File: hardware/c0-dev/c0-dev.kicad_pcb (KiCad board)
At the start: 2 copper layers, 316 parts, among them J1 RJHSE5385, J2 TAG_CONNECT, Q1 BSS138P, Q2 BSS138P, U1 LAN8720A, U10 ISO1540, U11 TMP117xxDRV, U12 AMS1117-3.3, U13 ADS1015IDGS, U14 ADS1015IDGS, U15 B0505S-1WR3, U16 ISO1540, U17 ADS1015IDGS, U18 ADS1015IDGS, U19 ADS1015IDGS, U2 TPS54360DDA, U20 ADS1015IDGS, U21 B0505S-1WR3, U22 ISO6741, U23 ISO6741, U24 ADS1220xPW, U25 ADS1220xPW, U26 B0505S-1WR3, U27 ISO1044BD, U28 TLP175A, U29 ISO1212, U3 TPS2378, U30 ISO1212, U31 ISO1212, U32 ISO1212, U4 TLP290, U5 B0505S-1WR3, U6 AMS1117-3.3, U7 W25Q128JVP, U8 RP2350A, U9 B0505S-1WR3, Y1 ABM8-272-T3 (12Mhz)

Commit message: i2c address check
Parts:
- added C116: 10uF, Capacitor_SMD:C_0805_2012Metric, F.Cu at (180.1, 61.6)
- added C117: 0.1uF, Capacitor_SMD:C_0402_1005Metric, F.Cu at (183.7, 61.1)
- added C118: 10uF, Capacitor_SMD:C_0805_2012Metric, F.Cu at (180.1, 64.6)
- added C119: 0.1uF, Capacitor_SMD:C_0402_1005Metric, F.Cu at (183.7, 63.1)
- added C120: 10uF, Capacitor_SMD:C_0805_2012Metric, F.Cu at (180.1, 67.7)
- added C121: 0.1uF, Capacitor_SMD:C_0402_1005Metric, F.Cu at (183.7, 65.1)
- added C122: 1uF, Capacitor_SMD:C_0603_1608Metric, F.Cu at (200.2, 89.1)
- added C123: 2.2uF, Capacitor_SMD:C_0603_1608Metric, F.Cu at (200.2, 91.6)
- added C124: 10uF, Capacitor_SMD:C_1206_3216Metric, F.Cu at (201.0, 94.6)
- added C125: 1uF, Capacitor_SMD:C_0603_1608Metric, F.Cu at (179.5, 81.9)
- added C126: 2.2uF, Capacitor_SMD:C_0603_1608Metric, F.Cu at (179.5, 84.4)
- added C127: 10uF, Capacitor_SMD:C_1206_3216Metric, F.Cu at (180.3, 87.4)
- added C128: 1uF, Capacitor_SMD:C_0603_1608Metric, F.Cu at (218.8, 71.9)
- added C129: 2.2uF, Capacitor_SMD:C_0603_1608Metric, F.Cu at (218.8, 74.4)
- added C130: 10uF, Capacitor_SMD:C_1206_3216Metric, F.Cu at (219.7, 77.4)
- added C131: 1uF, Capacitor_SMD:C_0603_1608Metric, F.Cu at (179.5, 99.1)
- added C132: 2.2uF, Capacitor_SMD:C_0603_1608Metric, F.Cu at (179.5, 101.6)
- added C133: 10uF, Capacitor_SMD:C_1206_3216Metric, F.Cu at (180.3, 104.5)
- added C134: 1uF, Capacitor_SMD:C_0603_1608Metric, F.Cu at (200.2, 71.9)
- added C135: 2.2uF, Capacitor_SMD:C_0603_1608Metric, F.Cu at (200.2, 74.4)
- added C136: 10uF, Capacitor_SMD:C_1206_3216Metric, F.Cu at (201.0, 77.4)
- added C137: 1uF, Capacitor_SMD:C_0603_1608Metric, F.Cu at (200.2, 54.7)
- added C138: 2.2uF, Capacitor_SMD:C_0603_1608Metric, F.Cu at (200.2, 57.3)
- added C139: 10uF, Capacitor_SMD:C_1206_3216Metric, F.Cu at (201.0, 60.2)
- added C140: 1uF, Capacitor_SMD:C_0603_1608Metric, F.Cu at (218.8, 89.1)
- added C141: 2.2uF, Capacitor_SMD:C_0603_1608Metric, F.Cu at (218.8, 91.6)
- added C142: 10uF, Capacitor_SMD:C_1206_3216Metric, F.Cu at (219.7, 94.6)
- added C143: 1uF, Capacitor_SMD:C_0603_1608Metric, F.Cu at (218.8, 54.7)
- added C144: 2.2uF, Capacitor_SMD:C_0603_1608Metric, F.Cu at (218.8, 57.3)
- added C145: 10uF, Capacitor_SMD:C_1206_3216Metric, F.Cu at (219.7, 60.2)
- added D36: SS14, Diode_SMD:D_SMA, F.Cu at (170.6, 69.0)
- added D37: SS14, Diode_SMD:D_SMA, F.Cu at (194.2, 90.1)
- added D38: PTVS30VP1UP, Diode_SMD:D_SOD-128, F.Cu at (193.8, 94.4)
- added D39: SS14, Diode_SMD:D_SMA, F.Cu at (173.5, 82.9)
- added D40: PTVS30VP1UP, Diode_SMD:D_SOD-128, F.Cu at (173.1, 87.2)
- added D41: SS14, Diode_SMD:D_SMA, F.Cu at (212.8, 73.0)
- added D42: PTVS30VP1UP, Diode_SMD:D_SOD-128, F.Cu at (212.5, 77.3)
- added D43: SS14, Diode_SMD:D_SMA, F.Cu at (173.5, 100.1)
- added D44: PTVS30VP1UP, Diode_SMD:D_SOD-128, F.Cu at (173.1, 104.4)
- added D45: SS14, Diode_SMD:D_SMA, F.Cu at (194.2, 73.0)
- added D46: PTVS30VP1UP, Diode_SMD:D_SOD-128, F.Cu at (193.8, 77.3)
- added D47: SS14, Diode_SMD:D_SMA, F.Cu at (194.2, 55.8)
- added D48: PTVS30VP1UP, Diode_SMD:D_SOD-128, F.Cu at (193.8, 60.1)
- added D49: SS14, Diode_SMD:D_SMA, F.Cu at (212.8, 90.1)
- added D50: PTVS30VP1UP, Diode_SMD:D_SOD-128, F.Cu at (212.5, 94.4)
- added D51: SS14, Diode_SMD:D_SMA, F.Cu at (212.8, 55.8)
- added D52: PTVS30VP1UP, Diode_SMD:D_SOD-128, F.Cu at (212.5, 60.1)
- added FB8: 600Ω@100MHz, Inductor_SMD:L_0603_1608Metric, F.Cu at (179.9, 70.4)
- added R103: 2k, Resistor_SMD:R_1206_3216Metric, F.Cu at (170.0, 116.1)
- added R109: 560, Resistor_SMD:R_0402_1005Metric, F.Cu at (174.3, 117.4)
- added R113: 2k, Resistor_SMD:R_1206_3216Metric, F.Cu at (170.0, 119.4)
- added R113: 1k, Resistor_SMD:R_0402_1005Metric, F.Cu at (176.4, 61.1)
- added R114: 1k, Resistor_SMD:R_0402_1005Metric, F.Cu at (176.4, 63.1)
- added R115: 1k, Resistor_SMD:R_0402_1005Metric, F.Cu at (176.4, 65.1)
- added R116: 1k, Resistor_SMD:R_0402_1005Metric, F.Cu at (176.4, 67.1)
- added R117: 1k, Resistor_SMD:R_0402_1005Metric, F.Cu at (176.4, 69.1)
- added R118: 1k, Resistor_SMD:R_0402_1005Metric, F.Cu at (176.4, 71.1)
- added R119: 10k, Resistor_SMD:R_0402_1005Metric, F.Cu at (188.6, 82.3)
- added R120: 715k, Resistor_SMD:R_0402_1005Metric, F.Cu at (188.6, 84.3)
- added R121: 20k, Resistor_SMD:R_0402_1005Metric, F.Cu at (188.6, 86.3)
- added R122: 30.1k, Resistor_SMD:R_0402_1005Metric, F.Cu at (188.6, 88.2)
- added R123: 0, Resistor_SMD:R_0402_1005Metric, F.Cu at (188.6, 90.2)
- added R124: 10k, Resistor_SMD:R_0402_1005Metric, F.Cu at (188.6, 92.2)
- added R125: 12k, Resistor_SMD:R_0402_1005Metric, F.Cu at (188.6, 94.2)
- added R126: 62k, Resistor_SMD:R_0402_1005Metric, F.Cu at (168.0, 75.1)
- added R127: 715k, Resistor_SMD:R_0402_1005Metric, F.Cu at (168.0, 77.1)
- added R128: 20k, Resistor_SMD:R_0402_1005Metric, F.Cu at (168.0, 79.0)
- added R129: 30.1k, Resistor_SMD:R_0402_1005Metric, F.Cu at (168.0, 81.0)
- added R13: 2M, Resistor_SMD:R_1206_3216Metric, F.Cu at (170.0, 132.9)
- added R130: 0, Resistor_SMD:R_0402_1005Metric, F.Cu at (168.0, 83.0)
- added R131: 10k, Resistor_SMD:R_0402_1005Metric, F.Cu at (168.0, 85.0)
- added R132: 12k, Resistor_SMD:R_0402_1005Metric, F.Cu at (168.0, 87.0)
- added R133: 62k, Resistor_SMD:R_0402_1005Metric, F.Cu at (207.3, 65.1)
- added R134: 715k, Resistor_SMD:R_0402_1005Metric, F.Cu at (207.3, 67.1)
- added R135: 20k, Resistor_SMD:R_0402_1005Metric, F.Cu at (207.3, 69.1)
- added R136: 30.1k, Resistor_SMD:R_0402_1005Metric, F.Cu at (207.3, 71.1)
- added R137: 0, Resistor_SMD:R_0402_1005Metric, F.Cu at (207.3, 73.0)
- added R138: 10k, Resistor_SMD:R_0402_1005Metric, F.Cu at (207.3, 75.0)
- added R139: 12k, Resistor_SMD:R_0402_1005Metric, F.Cu at (207.3, 77.0)
- added R140: 62k, Resistor_SMD:R_0402_1005Metric, F.Cu at (168.0, 92.3)
- added R141: 715k, Resistor_SMD:R_0402_1005Metric, F.Cu at (168.0, 94.2)
- added R142: 20k, Resistor_SMD:R_0402_1005Metric, F.Cu at (168.0, 96.2)
- added R143: 30.1k, Resistor_SMD:R_0402_1005Metric, F.Cu at (168.0, 98.2)
- added R144: 0, Resistor_SMD:R_0402_1005Metric, F.Cu at (168.0, 100.2)
- added R145: 10k, Resistor_SMD:R_0402_1005Metric, F.Cu at (168.0, 102.2)
- added R146: 12k, Resistor_SMD:R_0402_1005Metric, F.Cu at (168.0, 104.2)
- added R147: 62k, Resistor_SMD:R_0402_1005Metric, F.Cu at (188.6, 65.1)
- added R148: 715k, Resistor_SMD:R_0402_1005Metric, F.Cu at (188.6, 67.1)
- added R149: 20k, Resistor_SMD:R_0402_1005Metric, F.Cu at (188.6, 69.1)
- added R150: 30.1k, Resistor_SMD:R_0402_1005Metric, F.Cu at (188.6, 71.1)
- added R151: 0, Resistor_SMD:R_0402_1005Metric, F.Cu at (188.6, 73.0)
- added R152: 10k, Resistor_SMD:R_0402_1005Metric, F.Cu at (188.6, 75.0)
- added R153: 12k, Resistor_SMD:R_0402_1005Metric, F.Cu at (188.6, 77.0)
- added R154: 62k, Resistor_SMD:R_0402_1005Metric, F.Cu at (188.6, 47.9)
- added R155: 715k, Resistor_SMD:R_0402_1005Metric, F.Cu at (188.6, 49.9)
- added R156: 20k, Resistor_SMD:R_0402_1005Metric, F.Cu at (188.6, 51.9)
- added R157: 30.1k, Resistor_SMD:R_0402_1005Metric, F.Cu at (188.6, 53.9)
- added R158: 0, Resistor_SMD:R_0402_1005Metric, F.Cu at (188.6, 55.9)
- added R159: 10k, Resistor_SMD:R_0402_1005Metric, F.Cu at (188.6, 57.8)
- added R160: 12k, Resistor_SMD:R_0402_1005Metric, F.Cu at (188.6, 59.8)
- added R161: 62k, Resistor_SMD:R_0402_1005Metric, F.Cu at (207.3, 82.3)
- added R162: 715k, Resistor_SMD:R_0402_1005Metric, F.Cu at (207.3, 84.3)
- added R163: 20k, Resistor_SMD:R_0402_1005Metric, F.Cu at (207.3, 86.3)
- added R164: 30.1k, Resistor_SMD:R_0402_1005Metric, F.Cu at (207.3, 88.2)
- added R165: 0, Resistor_SMD:R_0402_1005Metric, F.Cu at (207.3, 90.2)
- added R166: 10k, Resistor_SMD:R_0402_1005Metric, F.Cu at (207.3, 92.2)
- added R167: 12k, Resistor_SMD:R_0402_1005Metric, F.Cu at (207.3, 94.2)
- added R168: 62k, Resistor_SMD:R_0402_1005Metric, F.Cu at (207.3, 47.9)
- added R169: 715k, Resistor_SMD:R_0402_1005Metric, F.Cu at (207.3, 49.9)
- added R170: 20k, Resistor_SMD:R_0402_1005Metric, F.Cu at (207.3, 51.9)
- added R171: 30.1k, Resistor_SMD:R_0402_1005Metric, F.Cu at (207.3, 53.9)
- added R172: 0, Resistor_SMD:R_0402_1005Metric, F.Cu at (207.3, 55.9)
- added R173: 10k, Resistor_SMD:R_0402_1005Metric, F.Cu at (207.3, 57.8)
- added R174: 12k, Resistor_SMD:R_0402_1005Metric, F.Cu at (207.3, 59.8)
- added R175: 62k, Resistor_SMD:R_0402_1005Metric, F.Cu at (184.4, 131.3)
- added R41: 1k, Resistor_SMD:R_0402_1005Metric, F.Cu at (178.0, 127.3)
- added R49: 2k, Resistor_SMD:R_1206_3216Metric, F.Cu at (179.3, 124.7)
- added R67: 1.6k, Resistor_SMD:R_0402_1005Metric, F.Cu at (173.1, 127.3)
- added R71: 160, Resistor_SMD:R_0805_2012Metric, F.Cu at (169.4, 127.8)
- added R72: 0, Resistor_SMD:R_1206_3216Metric, F.Cu at (170.0, 124.7)
- added R78: 1k, Resistor_SMD:R_0402_1005Metric, F.Cu at (184.8, 115.4)
- added R82: 2k, Resistor_SMD:R_1206_3216Metric, F.Cu at (180.5, 116.1)
- added R86: 1M, Resistor_SMD:R_0402_1005Metric, F.Cu at (184.8, 117.4)
- added R88: 2k, Resistor_SMD:R_1206_3216Metric, F.Cu at (180.5, 119.4)
- added R91: 1k, Resistor_SMD:R_0402_1005Metric, F.Cu at (178.0, 134.3)
- added R92: 120R, Resistor_SMD:R_0805_2012Metric, F.Cu at (178.7, 131.8)
- added R99: 560, Resistor_SMD:R_0402_1005Metric, F.Cu at (174.3, 115.4)
- added U33: B0505S-1WR3, Converter_DCDC:Converter_DCDC_Murata_MEE1SxxxxSC_THT, F.Cu at (168.6, 49.9)
- added U34: ISO1540, Package_SO:SOIC-8_3.9x4.9mm_P1.27mm, F.Cu at (170.7, 63.5)
- added U35: TCA9555PWR, Package_SO:TSSOP-24_4.4x7.8mm_P0.65mm, F.Cu at (179.1, 51.6)
- added U36: TPS26600PWP, Package_SO:HTSSOP-16-1EP_4.4x5mm_P0.65mm_EP3.4x5mm_Mask2.66x2.46mm_ThermalVias, F.Cu at (194.9, 84.6)
- added U37: TPS26600PWP, Package_SO:HTSSOP-16-1EP_4.4x5mm_P0.65mm_EP3.4x5mm_Mask2.66x2.46mm_ThermalVias, F.Cu at (174.2, 77.4)
- added U38: TPS26600PWP, Package_SO:HTSSOP-16-1EP_4.4x5mm_P0.65mm_EP3.4x5mm_Mask2.66x2.46mm_ThermalVias, F.Cu at (213.5, 67.4)
- added U39: TPS26600PWP, Package_SO:HTSSOP-16-1EP_4.4x5mm_P0.65mm_EP3.4x5mm_Mask2.66x2.46mm_ThermalVias, F.Cu at (174.2, 94.6)
- added U40: TPS26600PWP, Package_SO:HTSSOP-16-1EP_4.4x5mm_P0.65mm_EP3.4x5mm_Mask2.66x2.46mm_ThermalVias, F.Cu at (194.9, 67.4)
- added U41: TPS26600PWP, Package_SO:HTSSOP-16-1EP_4.4x5mm_P0.65mm_EP3.4x5mm_Mask2.66x2.46mm_ThermalVias, F.Cu at (194.9, 50.2)
- added U42: TPS26600PWP, Package_SO:HTSSOP-16-1EP_4.4x5mm_P0.65mm_EP3.4x5mm_Mask2.66x2.46mm_ThermalVias, F.Cu at (213.5, 84.6)
- added U43: TPS26600PWP, Package_SO:HTSSOP-16-1EP_4.4x5mm_P0.65mm_EP3.4x5mm_Mask2.66x2.46mm_ThermalVias, F.Cu at (213.5, 50.2)
- R105, R95: value 560 -> 1k
- R17: value 33R -> 75R
- R19: value 68.1k -> 33R
- R20: value 25k -> 68.1k
- R21: value 63.4R -> 25k
- R22: value 6.34k -> 63.4R
- R23: value 60.4k -> 6.34k
- R24: value 11.5k -> 60.4k
- R25: value 1k -> 11.5k
- R26: value 10k -> 1k
- R27, R74: value 1k -> 10k
- R28: value 33 -> 1k
- R29: value 1k -> 33
- R30: value DNP -> 1k
- R31: value 0 -> DNP
- R32: value 27 -> 0
- R33, R36: value 1k -> 27
- R35: value 27 -> 1k
- R57: value 1k -> 1M
- R63: value 1.6k -> 1k
- R90, R93: value 1k -> 0
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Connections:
- R100 pad 1: /Digital Input/IN1 -> /Digital Input/IN0
- R100 pad 2: Net-(U29-SENSE2) -> Net-(U29-SENSE1)
- R101 pad 1: /Digital Input/IN2 -> /Digital Input/IN1
- R101 pad 2: Net-(U30-SENSE1) -> Net-(U29-SENSE2)
- R102 pad 1: /Digital Input/IN3 -> /Digital Input/IN2
- R102 pad 2: Net-(U30-SENSE2) -> Net-(U30-SENSE1)
- R104 pad 2: Net-(U32-EN) -> Net-(U31-EN)
- R105 pad 1: Net-(U31-IN1) -> /Digital Input/+3.3V_ISO
- R105 pad 2: Net-(U31-SENSE1) -> Net-(U32-EN)
- R106 pad 1: Net-(U31-IN2) -> Net-(U31-IN1)
- R106 pad 2: Net-(U31-SENSE2) -> Net-(U31-SENSE1)
- R107 pad 1: Net-(U32-IN1) -> Net-(U31-IN2)
- R107 pad 2: Net-(U32-SENSE1) -> Net-(U31-SENSE2)
- R108 pad 1: Net-(U32-IN2) -> Net-(U32-IN1)
- R108 pad 2: Net-(U32-SENSE2) -> Net-(U32-SENSE1)
- R110 pad 1: /Digital Input/IN5 -> /Digital Input/IN4
- R110 pad 2: Net-(U31-SENSE2) -> Net-(U31-SENSE1)
- R111 pad 1: /Digital Input/IN6 -> /Digital Input/IN5
- R111 pad 2: Net-(U32-SENSE1) -> Net-(U31-SENSE2)
- R112 pad 1: /Digital Input/IN7 -> /Digital Input/IN6
- R112 pad 2: Net-(U32-SENSE2) -> Net-(U32-SENSE1)
- R14 pad 1: Net-(C9-Pad2) -> Net-(C8-Pad2)
- R15 pad 1: Net-(C10-Pad2) -> Net-(C9-Pad2)
- R16 pad 1: Net-(C11-Pad2) -> Net-(C10-Pad2)
- R17 pad 1: /Ethernet/LED1 -> Net-(C11-Pad2)
- R17 pad 2: Net-(J1-Pad11) -> Earth
- R18 pad 1: /Ethernet/LED2 -> /Ethernet/LED1
- R18 pad 2: Net-(J1-Pad9) -> Net-(J1-Pad11)
- R19 pad 1: Net-(U2-RT/CLK) -> /Ethernet/LED2
- R19 pad 2: GND_ISO -> Net-(J1-Pad9)
- R20 pad 1: Net-(U3-DEN) -> Net-(U2-RT/CLK)
- R20 pad 2: +POE -> GND_ISO
- R21 pad 1: -POE -> Net-(U3-DEN)
- R21 pad 2: Net-(U3-CLS) -> +POE
- R22 pad 1: Net-(U2-COMP) -> -POE
- R22 pad 2: Net-(C19-Pad1) -> Net-(U3-CLS)
- R23 pad 1: +5V_ISO -> Net-(U2-COMP)
- R23 pad 2: Net-(R23-Pad2) -> Net-(C19-Pad1)
- R24 pad 1: Net-(R23-Pad2) -> +5V_ISO
- R24 pad 2: GND_ISO -> Net-(R24-Pad2)
- R25 pad 1: GND_ISO -> Net-(R24-Pad2)
- R25 pad 2: Net-(U3-APD) -> GND_ISO
- R26 pad 1: +POE -> GND_ISO
- R26 pad 2: Net-(R26-Pad2) -> Net-(U3-APD)
- R27 pad 1: +3.3V -> +POE
- R27 pad 2: /Power/T2P -> Net-(R27-Pad2)
- R28 pad 2: /MCU/VREG_AVDD -> /Power/T2P
- R29 pad 1: Net-(R29-Pad1) -> +3.3V
- R29 pad 2: /MCU/~{QSPI_SS} -> /MCU/VREG_AVDD
- R30 pad 1: +3.3V -> Net-(R30-Pad1)
- R30 pad 2: Net-(U7-~{CS}) -> /MCU/~{QSPI_SS}
- R31 pad 1: Net-(U7-~{CS}) -> +3.3V
- R31 pad 2: /MCU/~{QSPI_SS} -> Net-(U7-~{CS})
- R32 pad 1: /MCU/USB_D+ -> Net-(U7-~{CS})
- R32 pad 2: Net-(U8-USB_DP) -> /MCU/~{QSPI_SS}
- R33 pad 1: Net-(C39-Pad2) -> /MCU/USB_D+
- R33 pad 2: Net-(U8-XOUT) -> Net-(U8-USB_DP)
- R34 pad 1: /MCU/~{RST} -> Net-(C39-Pad2)
- R34 pad 2: +3.3V -> Net-(U8-XOUT)
- R35 pad 1: /MCU/USB_D- -> /MCU/~{RST}
- R35 pad 2: Net-(U8-USB_DM) -> +3.3V
- R36 pad 1: /frontend_temp/SCL -> /MCU/USB_D-
- R36 pad 2: Net-(U11-ADD0) -> Net-(U8-USB_DM)
- R37 pad 2: /frontend_temp/+3.3V -> Net-(U11-ADD0)
- R38 pad 1: /frontend_temp/SDA -> /frontend_temp/SCL
- R39 pad 1: /frontend_temp/GND -> /frontend_temp/SDA
- R39 pad 2: Net-(U13-ADDR) -> /frontend_temp/+3.3V
- R40 pad 1: /frontend_temp/+3.3V -> /frontend_temp/GND
- R40 pad 2: Net-(U14-ADDR) -> Net-(U13-ADDR)
- R42 pad 1: /frontend_temp/TC0+ -> /frontend_temp/TC0-
- R42 pad 2: Net-(D6A-K3A4) -> Net-(D6B-K1A2)
- R43 pad 1: /frontend_temp/TC1- -> /frontend_temp/TC0+
- R43 pad 2: Net-(D7B-K1A2) -> Net-(D6A-K3A4)
- R44 pad 1: /frontend_temp/TC1+ -> /frontend_temp/TC1-
- R44 pad 2: Net-(D7A-K3A4) -> Net-(D7B-K1A2)
- R45 pad 1: /frontend_temp/TC2- -> /frontend_temp/TC1+
- R45 pad 2: Net-(D8B-K1A2) -> Net-(D7A-K3A4)
- R46 pad 1: /frontend_temp/TC2+ -> /frontend_temp/TC2-
- R46 pad 2: Net-(D8A-K3A4) -> Net-(D8B-K1A2)
- R47 pad 1: /frontend_temp/TC3- -> /frontend_temp/TC2+
- R47 pad 2: Net-(D9B-K1A2) -> Net-(D8A-K3A4)
- R48 pad 1: /frontend_temp/TC3+ -> /frontend_temp/TC3-
- R48 pad 2: Net-(D9A-K3A4) -> Net-(D9B-K1A2)
- R50 pad 1: /frontend_temp/GND -> /frontend_temp/TC0-
- R50 pad 2: /frontend_temp/TC0+ -> /frontend_temp/+3.3V
- R51 pad 1: /frontend_temp/TC1- -> /frontend_temp/GND
- R51 pad 2: /frontend_temp/+3.3V -> /frontend_temp/TC0+
- R52 pad 1: /frontend_temp/GND -> /frontend_temp/TC1-
- R52 pad 2: /frontend_temp/TC1+ -> /frontend_temp/+3.3V
- R53 pad 1: /frontend_temp/TC2- -> /frontend_temp/GND
- R53 pad 2: /frontend_temp/+3.3V -> /frontend_temp/TC1+
- R54 pad 1: /frontend_temp/GND -> /frontend_temp/TC2-
- R54 pad 2: /frontend_temp/TC2+ -> /frontend_temp/+3.3V
- R55 pad 1: /frontend_temp/TC3- -> /frontend_temp/GND
- R55 pad 2: /frontend_temp/+3.3V -> /frontend_temp/TC2+
- R56 pad 1: /frontend_temp/GND -> /frontend_temp/TC3-
- R56 pad 2: /frontend_temp/TC3+ -> /frontend_temp/+3.3V
- R57 pad 1: /frontend_420/SCL -> /frontend_temp/GND
- R57 pad 2: /frontend_420/+5V -> /frontend_temp/TC3+
- R58 pad 1: /frontend_420/SDA -> /frontend_420/SCL
- R59 pad 1: /frontend_420/GND -> /frontend_420/SDA
- R59 pad 2: Net-(U17-ADDR) -> /frontend_420/+5V
- R60 pad 1: /frontend_420/+5V -> /frontend_420/GND
- R60 pad 2: Net-(U18-ADDR) -> Net-(U17-ADDR)
- R61 pad 1: /frontend_420/SCL -> /frontend_420/+5V
- R61 pad 2: Net-(U19-ADDR) -> Net-(U18-ADDR)
- R62 pad 1: /frontend_420/SDA -> /frontend_420/SCL
- R62 pad 2: Net-(U20-ADDR) -> Net-(U19-ADDR)
- R63 pad 1: Net-(U17-AIN0) -> /frontend_420/SDA
- R63 pad 2: Net-(D19A-K3A4) -> Net-(U20-ADDR)
- R64 pad 1: Net-(U18-AIN0) -> Net-(U17-AIN0)
- R64 pad 2: Net-(D20A-K3A4) -> Net-(D19A-K3A4)
- R65 pad 1: Net-(U19-AIN0) -> Net-(U18-AIN0)
- R65 pad 2: Net-(D21A-K3A4) -> Net-(D20A-K3A4)
- R66 pad 1: Net-(U20-AIN0) -> Net-(U19-AIN0)
- R66 pad 2: Net-(D22A-K3A4) -> Net-(D21A-K3A4)
- R68 pad 1: Net-(D20A-K3A4) -> Net-(D19A-K3A4)
- R69 pad 1: Net-(D21A-K3A4) -> Net-(D20A-K3A4)
- R70 pad 1: Net-(D22A-K3A4) -> Net-(D21A-K3A4)
- R73 pad 2: /frontend_bridge/~{CS1_ISO} -> /frontend_bridge/~{CS0_ISO}
- R74 pad 1: Net-(U22-EN2) -> GND_ISO
- R74 pad 2: /frontend_bridge/+5V -> /frontend_bridge/~{CS1_ISO}
- R75 pad 1: Net-(U23-EN2) -> Net-(U22-EN2)
- R76 pad 1: /frontend_bridge/GND -> Net-(U23-EN2)
- R76 pad 2: Net-(U24-CLK) -> /frontend_bridge/+5V
- R77 pad 2: Net-(U25-CLK) -> Net-(U24-CLK)
- R79 pad 1: /frontend_bridge/B0- -> /frontend_bridge/B0+
- R79 pad 2: /frontend_bridge/AIN20 -> /frontend_bridge/AIN10
- R80 pad 1: /frontend_bridge/B1+ -> /frontend_bridge/B0-
- R80 pad 2: /frontend_bridge/AIN11 -> /frontend_bridge/AIN20
- R81 pad 1: /frontend_bridge/B1- -> /frontend_bridge/B1+
- R81 pad 2: /frontend_bridge/AIN21 -> /frontend_bridge/AIN11
- R83 pad 1: /frontend_bridge/GND -> /frontend_bridge/B0+
- R83 pad 2: /frontend_bridge/B0- -> /frontend_bridge/+5V
- R84 pad 1: /frontend_bridge/B1+ -> /frontend_bridge/GND
- R84 pad 2: /frontend_bridge/+5V -> /frontend_bridge/B0-
- R85 pad 1: /frontend_bridge/GND -> /frontend_bridge/B1+
- R85 pad 2: /frontend_bridge/B1- -> /frontend_bridge/+5V
- R87 pad 1: /frontend_bridge/B1_5V+ -> /frontend_bridge/B0_5V+
- R87 pad 2: /frontend_bridge/+5V_SENSE1 -> /frontend_bridge/+5V_SENSE0
- R89 pad 1: /frontend_bridge/B1_GND -> /frontend_bridge/B0_GND
- R90 pad 1: Net-(R90-Pad1) -> /frontend_bridge/B1_GND
- R90 pad 2: /CAN/TERM_EN -> /frontend_bridge/GND
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
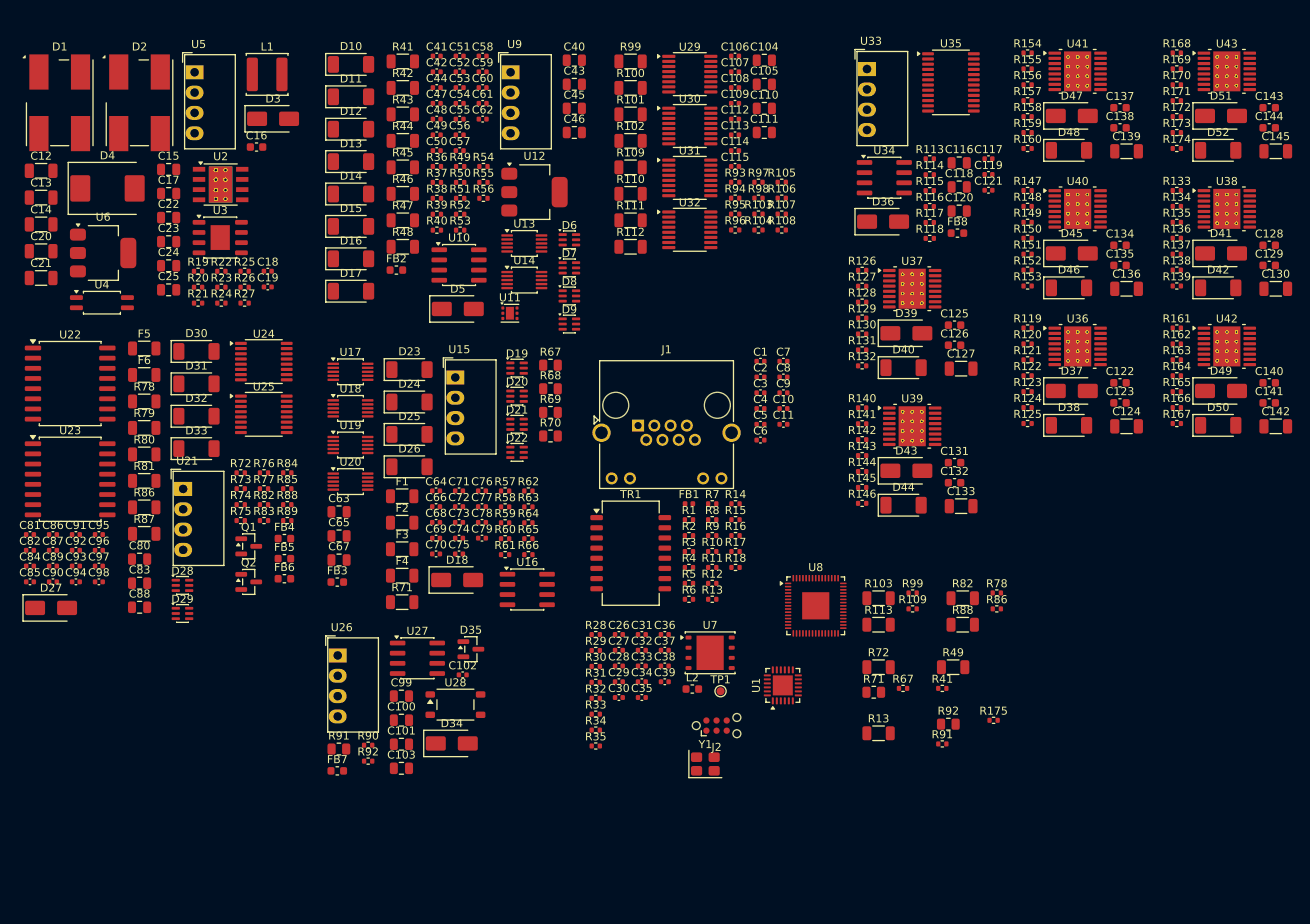
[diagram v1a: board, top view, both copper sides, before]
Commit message: added connectors
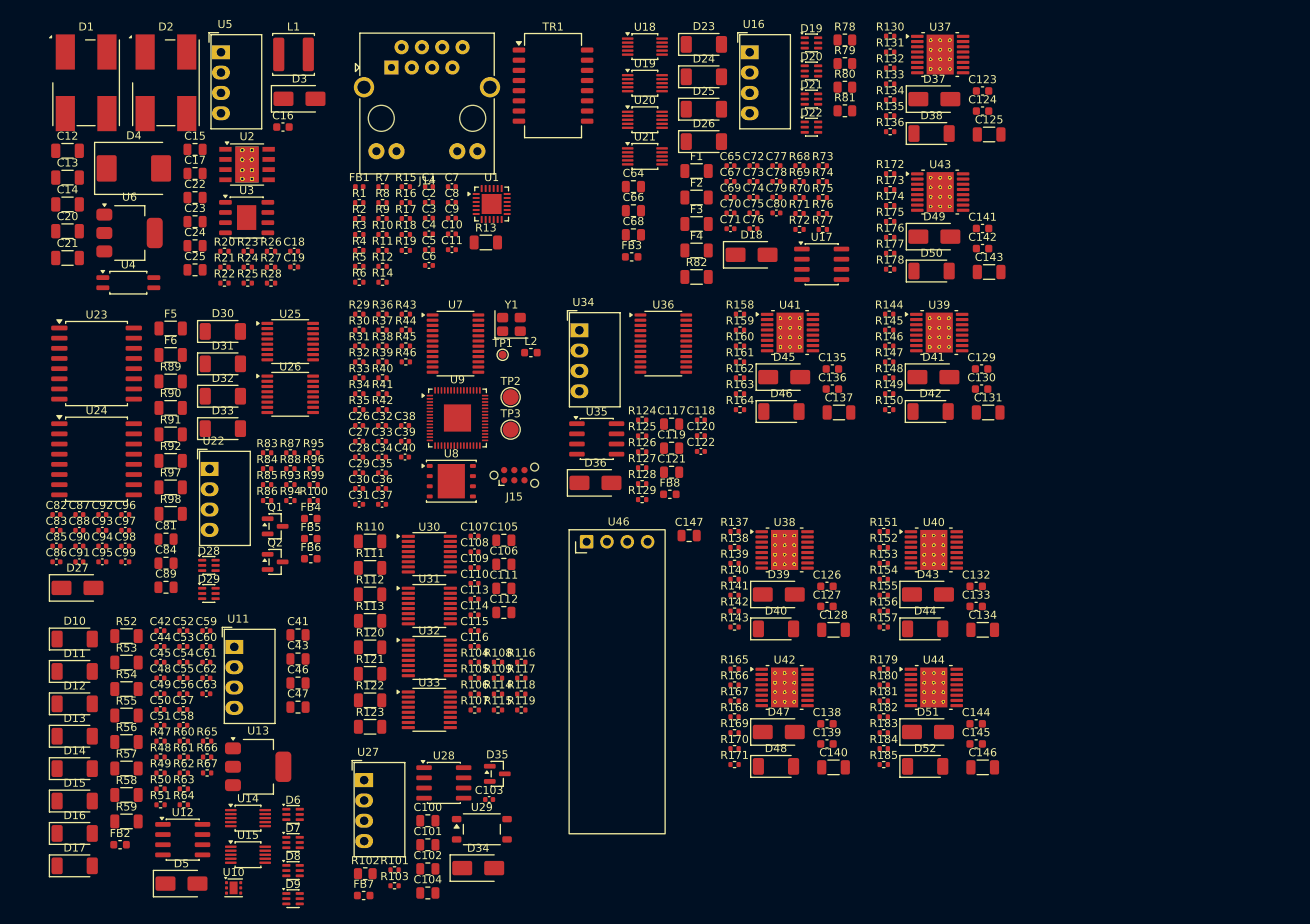
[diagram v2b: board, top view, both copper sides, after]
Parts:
- removed J1: RJHSE5385, Connector_RJ:RJ45_Amphenol_RJHSE538X
- removed J2: TAG_CONNECT, Connector:Tag-Connect_TC2030-IDC-NL_2x03_P1.27mm_Vertical
- removed the R103 at (170.0, 116.1)
- removed the R103 at (155.0, 68.0)
- removed the R109 at (139.0, 62.2)
- removed the R109 at (174.3, 117.4)
- removed the R113 at (170.0, 119.4)
- removed the R113 at (176.4, 61.1)
- removed the R13 at (170.0, 132.9)
- removed the R13 at (149.2, 116.2)
- removed the R41 at (178.0, 127.3)
- removed the R41 at (110.5, 49.0)
- removed the R49 at (117.7, 62.1)
- removed the R49 at (179.3, 124.7)
- removed the R67 at (129.0, 86.9)
- removed the R67 at (173.1, 127.3)
- removed the R71 at (169.4, 127.8)
- removed the R71 at (110.5, 116.5)
- removed the R72 at (170.0, 124.7)
- removed the R72 at (90.3, 100.4)
- removed the R78 at (184.8, 115.4)
- removed the R78 at (78.2, 91.5)
- removed the R82 at (180.5, 116.1)
- removed the R82 at (93.2, 104.4)
- removed the R86 at (78.2, 104.7)
- removed the R86 at (184.8, 117.4)
- removed the R88 at (180.5, 119.4)
- removed the R88 at (96.1, 104.4)
- removed the R91 at (102.5, 134.9)
- removed the R91 at (178.0, 134.3)
- removed the R92 at (106.2, 136.4)
- removed the R92 at (178.7, 131.8)
- removed the R99 at (139.0, 49.0)
- removed the R99 at (174.3, 115.4)
- added C146: 10uF, Capacitor_SMD:C_1206_3216Metric, F.Cu at (183.0, 137.2)
- added C147: 10uF, Capacitor_SMD:C_0805_2012Metric, F.Cu at (146.3, 108.2)
- added J14: RJ45_LED_Shielded, Connector_RJ:RJ45_BEL_SS74301-00x_Vertical, F.Cu at (109.1, 49.7)
- added J15: TAG_CONNECT, Connector:Tag-Connect_TC2030-IDC-NL_2x03_P1.27mm_Vertical, F.Cu at (124.5, 100.7)
- added R103: 0, Resistor_SMD:R_0402_1005Metric, F.Cu at (109.5, 152.0)
- added R109: 560, Resistor_SMD:R_0402_1005Metric, F.Cu at (122.4, 126.0)
- added R113: 2k, Resistor_SMD:R_1206_3216Metric, F.Cu at (106.4, 118.9)
- added R13: 2M, Resistor_SMD:R_1206_3216Metric, F.Cu at (120.9, 71.6)
- added R176: 10k, Resistor_SMD:R_0402_1005Metric, F.Cu at (171.5, 70.9)
- added R177: 12k, Resistor_SMD:R_0402_1005Metric, F.Cu at (171.5, 72.9)
- added R178: 62k, Resistor_SMD:R_0402_1005Metric, F.Cu at (171.5, 74.9)
- added R179: 715k, Resistor_SMD:R_0402_1005Metric, F.Cu at (170.7, 124.9)
- added R180: 20k, Resistor_SMD:R_0402_1005Metric, F.Cu at (170.7, 126.9)
- added R181: 30.1k, Resistor_SMD:R_0402_1005Metric, F.Cu at (170.7, 128.9)
- added R182: 0, Resistor_SMD:R_0402_1005Metric, F.Cu at (170.7, 130.9)
- added R183: 10k, Resistor_SMD:R_0402_1005Metric, F.Cu at (170.7, 132.9)
- added R184: 12k, Resistor_SMD:R_0402_1005Metric, F.Cu at (170.7, 134.9)
- added R185: 62k, Resistor_SMD:R_0402_1005Metric, F.Cu at (170.7, 136.8)
- added R41: 1k, Resistor_SMD:R_0402_1005Metric, F.Cu at (108.0, 90.5)
- added R49: 1k, Resistor_SMD:R_0402_1005Metric, F.Cu at (80.3, 137.9)
- added R67: 1M, Resistor_SMD:R_0402_1005Metric, F.Cu at (86.1, 137.9)
- added R71: 1k, Resistor_SMD:R_0402_1005Metric, F.Cu at (160.1, 68.0)
- added R72: 1k, Resistor_SMD:R_0402_1005Metric, F.Cu at (160.1, 70.0)
- added R78: 160, Resistor_SMD:R_0805_2012Metric, F.Cu at (165.8, 46.3)
- added R82: 0, Resistor_SMD:R_1206_3216Metric, F.Cu at (147.3, 75.9)
- added R86: 1k, Resistor_SMD:R_0402_1005Metric, F.Cu at (93.6, 103.8)
- added R88: 1k, Resistor_SMD:R_0402_1005Metric, F.Cu at (96.5, 99.9)
- added R91: 2k, Resistor_SMD:R_1206_3216Metric, F.Cu at (81.5, 95.6)
- added R92: 2k, Resistor_SMD:R_1206_3216Metric, F.Cu at (81.5, 98.9)
- added R99: 0, Resistor_SMD:R_0402_1005Metric, F.Cu at (99.4, 101.9)
- added TP2: TestPoint, TestPoint:TestPoint_Pad_D2.0mm, F.Cu at (124.0, 90.9)
- added TP3: TestPoint, TestPoint:TestPoint_Pad_D2.0mm, F.Cu at (124.0, 95.0)
- added U44: TPS26600PWP, Package_SO:HTSSOP-16-1EP_4.4x5mm_P0.65mm_EP3.4x5mm_Mask2.66x2.46mm_ThermalVias, F.Cu at (176.9, 127.2)
- added U46: ER_OLEDM0.91_1x-I2C, Display:ER_OLEDM0.91_1x-I2C, F.Cu at (133.5, 109.0)
- C102, C117, C119, C121, C41, C64, C66, C81, C84, C89: value 0.1uF -> 10uF; footprint Capacitor_SMD:C_0402_1005Metric -> Capacitor_SMD:C_0805_2012Metric
- C103, C118, C120, C45, C63, C65, C67, C80, C83, C88, C99: value 10uF -> 0.1uF; footprint Capacitor_SMD:C_0805_2012Metric -> Capacitor_SMD:C_0402_1005Metric
- C106, C112: value 1nF -> 10uF; footprint Capacitor_SMD:C_0402_1005Metric -> Capacitor_SMD:C_0805_2012Metric
- C110, C116: value 10uF -> 1nF; footprint Capacitor_SMD:C_0805_2012Metric -> Capacitor_SMD:C_0402_1005Metric
- C122: value 1uF -> 0.1uF; footprint Capacitor_SMD:C_0603_1608Metric -> Capacitor_SMD:C_0402_1005Metric
- C123, C126, C129, C132, C135, C138, C141, C144: value 2.2uF -> 1uF
- C124, C127, C130, C133, C136, C139, C142, C145: value 10uF -> 2.2uF; footprint Capacitor_SMD:C_1206_3216Metric -> Capacitor_SMD:C_0603_1608Metric
- C125, C128, C131, C134, C137, C140, C143: value 1uF -> 10uF; footprint Capacitor_SMD:C_0603_1608Metric -> Capacitor_SMD:C_1206_3216Metric
- C26: value 4.7u -> 0.1uF
- C28, C34, C37: value 0.1u -> 4.7u
- C33, C36: value 4.7u -> 0.1u
- C38: value 15p -> 0.1u
- C40: value 10uF -> 15p; footprint Capacitor_SMD:C_0805_2012Metric -> Capacitor_SMD:C_0402_1005Metric
- C47, C68: value 1uF -> 10uF; footprint Capacitor_SMD:C_0402_1005Metric -> Capacitor_SMD:C_0805_2012Metric
- C49, C72: value 0.1uF -> 1uF
- R100: value 2k -> 0; footprint Resistor_SMD:R_1206_3216Metric -> Resistor_SMD:R_0402_1005Metric
- R101, R42, R43, R44, R45, R46, R47, R48, R87: value 2k -> 1k; footprint Resistor_SMD:R_1206_3216Metric -> Resistor_SMD:R_0402_1005Metric
- R102: value 2k -> 120R; footprint Resistor_SMD:R_1206_3216Metric -> Resistor_SMD:R_0805_2012Metric
- R116, R117, R118: value 1k -> 560
- R119: value 10k -> 560
- R120: value 715k -> 2k; footprint Resistor_SMD:R_0402_1005Metric -> Resistor_SMD:R_1206_3216Metric
- R121: value 20k -> 2k; footprint Resistor_SMD:R_0402_1005Metric -> Resistor_SMD:R_1206_3216Metric
- R122: value 30.1k -> 2k; footprint Resistor_SMD:R_0402_1005Metric -> Resistor_SMD:R_1206_3216Metric
- R123, R89, R90: value 0 -> 2k; footprint Resistor_SMD:R_0402_1005Metric -> Resistor_SMD:R_1206_3216Metric
- R124, R73: value 10k -> 1k
- R125: value 12k -> 1k
- R126: value 62k -> 1k
- R127: value 715k -> 1k
- R128: value 20k -> 1k
- R129: value 30.1k -> 10k
- R130, R137, R144, R151, R158, R165, R172: value 0 -> 715k
- R131, R138, R145, R152, R159, R166, R173: value 10k -> 20k
- R132, R139, R146, R153, R160, R167, R174: value 12k -> 30.1k
- R133, R140, R147, R154, R161, R168, R175: value 62k -> 0
- R134, R141, R148, R155, R162, R169: value 715k -> 10k
- R135, R142, R149, R156, R163, R170: value 20k -> 12k
- R136, R143, R150, R157, R164, R171: value 30.1k -> 62k
- R29: value 33 -> 1k
- R31: value DNP -> 1k
- R32: value 0 -> 10k
- R33: value 27 -> 33
- R35: value 1k -> DNP
- R36: value 27 -> 0
- R37, R40: value 1k -> 27
- R50, R51, R85: value 1M -> 1k
- R52, R53, R54, R55, R56, R57: value 1M -> 2k; footprint Resistor_SMD:R_0402_1005Metric -> Resistor_SMD:R_1206_3216Metric
- R58, R59: value 1k -> 2k; footprint Resistor_SMD:R_0402_1005Metric -> Resistor_SMD:R_1206_3216Metric
- R60, R61, R62, R63, R94, R95: value 1k -> 1M
- R64, R65, R66: value 1.6k -> 1M
- R68, R69, R70: value 160 -> 1k; footprint Resistor_SMD:R_0805_2012Metric -> Resistor_SMD:R_0402_1005Metric
- R74: value 10k -> 1.6k
- R75, R76, R77: value 1k -> 1.6k
- R79, R80, R81: value 2k -> 160; footprint Resistor_SMD:R_1206_3216Metric -> Resistor_SMD:R_0805_2012Metric
- R83, R84: value 1M -> 10k
- R93: value 0 -> 1M
- R96: value 560 -> 1M
- R97, R98: value 560 -> 2k; footprint Resistor_SMD:R_0402_1005Metric -> Resistor_SMD:R_1206_3216Metric
- U10: value ISO1540 -> TMP117xxDRV; footprint Package_SO:SOIC-8_3.9x4.9mm_P1.27mm -> Package_SON:WSON-6-1EP_2x2mm_P0.65mm_EP1x1.6mm
- U11: value TMP117xxDRV -> B0505S-1WR3; footprint Package_SON:WSON-6-1EP_2x2mm_P0.65mm_EP1x1.6mm -> Converter_DCDC:Converter_DCDC_Murata_MEE1SxxxxSC_THT
- U12: value AMS1117-3.3 -> ISO1540; footprint Package_TO_SOT_SMD:SOT-223-3_TabPin2 -> Package_SO:SOIC-8_3.9x4.9mm_P1.27mm
- U13: value ADS1015IDGS -> AMS1117-3.3; footprint Package_SO:TSSOP-10_3x3mm_P0.5mm -> Package_TO_SOT_SMD:SOT-223-3_TabPin2
- U15, U21: value B0505S-1WR3 -> ADS1015IDGS; footprint Converter_DCDC:Converter_DCDC_Murata_MEE1SxxxxSC_THT -> Package_SO:TSSOP-10_3x3mm_P0.5mm
- U16, U34: value ISO1540 -> B0505S-1WR3; footprint Package_SO:SOIC-8_3.9x4.9mm_P1.27mm -> Converter_DCDC:Converter_DCDC_Murata_MEE1SxxxxSC_THT
- U17: value ADS1015IDGS -> ISO1540; footprint Package_SO:TSSOP-10_3x3mm_P0.5mm -> Package_SO:SOIC-8_3.9x4.9mm_P1.27mm
- U22: value ISO6741 -> B0505S-1WR3; footprint Package_SO:SOIC-16W_7.5x10.3mm_P1.27mm -> Converter_DCDC:Converter_DCDC_Murata_MEE1SxxxxSC_THT
- U24: value ADS1220xPW -> ISO6741; footprint Package_SO:TSSOP-16_4.4x5mm_P0.65mm -> Package_SO:SOIC-16W_7.5x10.3mm_P1.27mm
- U26: value B0505S-1WR3 -> ADS1220xPW; footprint Converter_DCDC:Converter_DCDC_Murata_MEE1SxxxxSC_THT -> Package_SO:TSSOP-16_4.4x5mm_P0.65mm
- U27: value ISO1044BD -> B0505S-1WR3; footprint Package_SO:SOIC-8_3.9x4.9mm_P1.27mm -> Converter_DCDC:Converter_DCDC_Murata_MEE1SxxxxSC_THT
- U28: value TLP175A -> ISO1044BD; footprint Package_SO:Toshiba_SOIC-4-6_4.4x3.6mm_P1.27mm -> Package_SO:SOIC-8_3.9x4.9mm_P1.27mm
- U29: value ISO1212 -> TLP175A; footprint Package_SO:SSOP-16_3.9x4.9mm_P0.635mm -> Package_SO:Toshiba_SOIC-4-6_4.4x3.6mm_P1.27mm
- U33: value B0505S-1WR3 -> ISO1212; footprint Converter_DCDC:Converter_DCDC_Murata_MEE1SxxxxSC_THT -> Package_SO:SSOP-16_3.9x4.9mm_P0.635mm
- U35: value TCA9555PWR -> ISO1540; footprint Package_SO:TSSOP-24_4.4x7.8mm_P0.65mm -> Package_SO:SOIC-8_3.9x4.9mm_P1.27mm
- U36: value TPS26600PWP -> TCA9555PWR; footprint Package_SO:HTSSOP-16-1EP_4.4x5mm_P0.65mm_EP3.4x5mm_Mask2.66x2.46mm_ThermalVias -> Package_SO:TSSOP-24_4.4x7.8mm_P0.65mm
- U7: value W25Q128JVP -> TCA9555PWR; footprint Package_SON:WSON-8-1EP_6x5mm_P1.27mm_EP3.4x4.3mm -> Package_SO:TSSOP-24_4.4x7.8mm_P0.65mm
- U8: value RP2350A -> W25Q128JVP; footprint Package_DFN_QFN:QFN-60-1EP_7x7mm_P0.4mm_EP3.4x3.4mm -> Package_SON:WSON-8-1EP_6x5mm_P1.27mm_EP3.4x4.3mm
- U9: value B0505S-1WR3 -> RP2350A; footprint Converter_DCDC:Converter_DCDC_Murata_MEE1SxxxxSC_THT -> Package_DFN_QFN:QFN-60-1EP_7x7mm_P0.4mm_EP3.4x3.4mm
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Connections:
- C100 pad 1: /CAN/+3.3V_ISO -> +5V_ISO
- C101 pad 1: Net-(U26-+Vout) -> +3.3V
- C101 pad 2: /CAN/GND -> GND
- C102 pad 1: /CAN/+5V -> Net-(U27-+Vout)
- C102 pad 2: /CAN/GND -> GND
- C103 pad 2: /CAN/GND -> GND
- C104 pad 1: /Digital Input/+3.3V_ISO -> /CAN/+5V
- C104 pad 2: /Digital Input/GND_ISO -> GND
- C105 pad 1: /Digital Input/+3.3V_ISO -> +3.3V
- C105 pad 2: /Digital Input/GND_ISO -> GND
- C106 pad 1: Net-(U29-SENSE1) -> +3.3V
- C106 pad 2: /Digital Input/GND_IN -> GND
- C107 pad 1: Net-(U29-SENSE2) -> Net-(U30-SENSE1)
- C108 pad 1: Net-(U30-SENSE1) -> Net-(U30-SENSE2)
- C109 pad 1: Net-(U30-SENSE2) -> Net-(U31-SENSE1)
- C110 pad 1: /Digital Input/+3.3V_ISO -> Net-(U31-SENSE2)
- C110 pad 2: /Digital Input/GND_ISO -> /Digital Input/GND_IN
- C111 pad 1: /Digital Input/+3.3V_ISO -> +3.3V
- C111 pad 2: /Digital Input/GND_ISO -> GND
- C112 pad 1: Net-(U31-SENSE1) -> +3.3V
- C112 pad 2: /Digital Input/GND_IN -> GND
- C113 pad 1: Net-(U31-SENSE2) -> Net-(U32-SENSE1)
- C114 pad 1: Net-(U32-SENSE1) -> Net-(U32-SENSE2)
- C115 pad 1: Net-(U32-SENSE2) -> Net-(U33-SENSE1)
- C116 pad 1: +5V_ISO -> Net-(U33-SENSE2)
- C116 pad 2: GND_ISO -> /Digital Input/GND_IN
- C117 pad 1: /Digital Output/+3.3V_ISO -> +5V_ISO
- C118 pad 1: Net-(U33-+Vout) -> +3.3V
- C118 pad 2: /Digital Output/GND -> GND
- C119 pad 1: /Digital Output/+5V -> Net-(U34-+Vout)
- C119 pad 2: /Digital Output/GND -> GND
- C120 pad 2: /Digital Output/GND -> GND
- C121 pad 2: /Digital Output/GND -> GND
- C122 pad 1: /Digital Output/24V -> /Digital Output/+5V
- C122 pad 2: /Digital Output/GND -> GND
- C123 pad 1: Net-(U36-dVdT) -> /Digital Output/24V
- C123 pad 2: /Digital Output/Highside Switch/RTN -> GND
- C124 pad 1: /Digital Output/OUT0 -> Net-(U37-dVdT)
- C124 pad 2: /Digital Output/GND -> /Digital Output/Highside Switch/RTN
- C125 pad 1: /Digital Output/24V -> /Digital Output/OUT0
- C125 pad 2: /Digital Output/GND -> GND
- C126 pad 1: Net-(U37-dVdT) -> /Digital Output/24V
- C126 pad 2: /Digital Output/Highside Switch1/RTN -> GND
- C127 pad 1: /Digital Output/OUT1 -> Net-(U38-dVdT)
- C127 pad 2: /Digital Output/GND -> /Digital Output/Highside Switch1/RTN
- C128 pad 1: /Digital Output/24V -> /Digital Output/OUT1
- C128 pad 2: /Digital Output/GND -> GND
- C129 pad 1: Net-(U38-dVdT) -> /Digital Output/24V
- C129 pad 2: /Digital Output/Highside Switch2/RTN -> GND
- C130 pad 1: /Digital Output/OUT2 -> Net-(U39-dVdT)
- C130 pad 2: /Digital Output/GND -> /Digital Output/Highside Switch2/RTN
- C131 pad 1: /Digital Output/24V -> /Digital Output/OUT2
- C131 pad 2: /Digital Output/GND -> GND
- C132 pad 1: Net-(U39-dVdT) -> /Digital Output/24V
- C132 pad 2: /Digital Output/Highside Switch3/RTN -> GND
- C133 pad 1: /Digital Output/OUT3 -> Net-(U40-dVdT)
- C133 pad 2: /Digital Output/GND -> /Digital Output/Highside Switch3/RTN
- C134 pad 1: /Digital Output/24V -> /Digital Output/OUT3
- C134 pad 2: /Digital Output/GND -> GND
- C135 pad 1: Net-(U40-dVdT) -> /Digital Output/24V
- C135 pad 2: /Digital Output/Highside Switch4/RTN -> GND
- C136 pad 1: /Digital Output/OUT4 -> Net-(U41-dVdT)
- C136 pad 2: /Digital Output/GND -> /Digital Output/Highside Switch4/RTN
- C137 pad 1: /Digital Output/24V -> /Digital Output/OUT4
- C137 pad 2: /Digital Output/GND -> GND
- C138 pad 1: Net-(U41-dVdT) -> /Digital Output/24V
- C138 pad 2: /Digital Output/Highside Switch5/RTN -> GND
- C139 pad 1: /Digital Output/OUT5 -> Net-(U42-dVdT)
- C139 pad 2: /Digital Output/GND -> /Digital Output/Highside Switch5/RTN
- C140 pad 1: /Digital Output/24V -> /Digital Output/OUT5
- C140 pad 2: /Digital Output/GND -> GND
- C141 pad 1: Net-(U42-dVdT) -> /Digital Output/24V
- C141 pad 2: /Digital Output/Highside Switch6/RTN -> GND
- C142 pad 1: /Digital Output/OUT6 -> Net-(U43-dVdT)
- C142 pad 2: /Digital Output/GND -> /Digital Output/Highside Switch6/RTN
- C143 pad 1: /Digital Output/24V -> /Digital Output/OUT6
- C143 pad 2: /Digital Output/GND -> GND
- C144 pad 1: Net-(U43-dVdT) -> /Digital Output/24V
- C144 pad 2: /Digital Output/Highside Switch7/RTN -> GND
- C145 pad 1: /Digital Output/OUT7 -> Net-(U44-dVdT)
- C145 pad 2: /Digital Output/GND -> /Digital Output/Highside Switch7/RTN
- C26 pad 1: +1.1V -> +3.3V
- C28 pad 1: +3.3V -> +1.1V
- C29 pad 1: +1.1V -> +3.3V
- C30 pad 1: +3.3V -> +1.1V
- C31 pad 1: +1.1V -> +3.3V
- C32 pad 1: +3.3V -> +1.1V
- C36 pad 1: /MCU/VREG_AVDD -> +3.3V
- C37 pad 1: +3.3V -> /MCU/VREG_AVDD
- C38 pad 1: GND -> +3.3V
- C38 pad 2: Net-(U8-XIN) -> GND
- C39 pad 2: Net-(C39-Pad2) -> Net-(U9-XIN)
- C40 pad 1: +5V_ISO -> GND
- C40 pad 2: GND_ISO -> Net-(C40-Pad2)
- C41 pad 1: /frontend_temp/+3.3V_ISO -> +5V_ISO
- C42 pad 1: /frontend_temp/+3.3V -> +3.3V
- C42 pad 2: /frontend_temp/GND -> GND
- C43 pad 2: /frontend_temp/GND -> GND
- C44 pad 1: /frontend_temp/+3.3V -> +3.3V
- C44 pad 2: /frontend_temp/GND -> GND
- C45 pad 1: Net-(D5-A) -> +3.3V
- C45 pad 2: /frontend_temp/GND -> GND
- C46 pad 1: /frontend_temp/+3.3V -> Net-(D5-A)
- C46 pad 2: /frontend_temp/GND -> GND
- C47 pad 1: /frontend_temp/+3.3V -> +3.3V
- C47 pad 2: /frontend_temp/GND -> GND
- C48 pad 1: /frontend_temp/+3.3V -> +3.3V
- C48 pad 2: /frontend_temp/GND -> GND
- C49 pad 1: /frontend_temp/+3.3V -> +3.3V
- C49 pad 2: /frontend_temp/GND -> GND
- C50 pad 1: /frontend_temp/+3.3V -> +3.3V
- C50 pad 2: /frontend_temp/GND -> GND
- C51 pad 1: Net-(D6B-K1A2) -> +3.3V
- C51 pad 2: /frontend_temp/GND -> GND
- C52 pad 2: Net-(D6A-K3A4) -> GND
- C53 pad 1: Net-(D6A-K3A4) -> Net-(D6B-K1A2)
- C53 pad 2: /frontend_temp/GND -> Net-(D6A-K3A4)
- C54 pad 1: Net-(D7B-K1A2) -> Net-(D6A-K3A4)
- C54 pad 2: /frontend_temp/GND -> GND
- C55 pad 2: Net-(D7A-K3A4) -> GND
- C56 pad 1: Net-(D7A-K3A4) -> Net-(D7B-K1A2)
- C56 pad 2: /frontend_temp/GND -> Net-(D7A-K3A4)
- C57 pad 1: Net-(D8B-K1A2) -> Net-(D7A-K3A4)
- C57 pad 2: /frontend_temp/GND -> GND
- C58 pad 2: Net-(D8A-K3A4) -> GND
- C59 pad 1: Net-(D8A-K3A4) -> Net-(D8B-K1A2)
- C59 pad 2: /frontend_temp/GND -> Net-(D8A-K3A4)
- C60 pad 1: Net-(D9B-K1A2) -> Net-(D8A-K3A4)
- C60 pad 2: /frontend_temp/GND -> GND
- C61 pad 2: Net-(D9A-K3A4) -> GND
- C62 pad 1: Net-(D9A-K3A4) -> Net-(D9B-K1A2)
- C62 pad 2: /frontend_temp/GND -> Net-(D9A-K3A4)
- C63 pad 1: +5V_ISO -> Net-(D9A-K3A4)
- C63 pad 2: GND_ISO -> GND
- C64 pad 1: /frontend_420/+3.3V_ISO -> +5V_ISO
- C65 pad 1: Net-(U15-+Vout) -> +3.3V
- C65 pad 2: /frontend_420/GND -> GND
- C66 pad 1: /frontend_420/+5V -> Net-(U16-+Vout)
- C66 pad 2: /frontend_420/GND -> GND
- C67 pad 2: /frontend_420/GND -> GND
- C68 pad 2: /frontend_420/GND -> GND
- C69 pad 2: /frontend_420/GND -> GND
- C70 pad 2: /frontend_420/GND -> GND
- C71 pad 2: /frontend_420/GND -> GND
- C72 pad 2: /frontend_420/GND -> GND
- C73 pad 2: /frontend_420/GND -> GND
- C74 pad 2: /frontend_420/GND -> GND
- C75 pad 2: /frontend_420/GND -> GND
- C76 pad 1: /frontend_420/GND -> /frontend_420/+5V
- C76 pad 2: Net-(U17-AIN0) -> GND
- C77 pad 1: /frontend_420/GND -> GND
- C78 pad 1: /frontend_420/GND -> GND
- C79 pad 1: /frontend_420/GND -> GND
- C80 pad 1: +5V_ISO -> GND
- C80 pad 2: GND_ISO -> Net-(U21-AIN0)
- C81 pad 1: /frontend_bridge/+3.3V_ISO -> +5V_ISO
- C82 pad 1: /frontend_bridge/+3.3V_ISO -> +3.3V
- C82 pad 2: GND_ISO -> GND
- C83 pad 1: Net-(U21-+Vout) -> +3.3V
- C83 pad 2: /frontend_bridge/GND -> GND
- C84 pad 1: /frontend_bridge/+5V -> Net-(U22-+Vout)
- C84 pad 2: /frontend_bridge/GND -> GND
- C85 pad 2: /frontend_bridge/GND -> GND
- C86 pad 2: /frontend_bridge/GND -> GND
- C87 pad 2: /frontend_bridge/GND -> GND
- C88 pad 2: /frontend_bridge/GND -> GND
- C89 pad 1: Net-(U24-DVDD) -> /frontend_bridge/+5V
- C89 pad 2: /frontend_bridge/GND -> GND
- C90 pad 2: /frontend_bridge/GND -> GND
- C91 pad 1: /frontend_bridge/+5V_SENSE0 -> Net-(U26-DVDD)
- C91 pad 2: Net-(U24-AIN3/REFN1) -> GND
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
